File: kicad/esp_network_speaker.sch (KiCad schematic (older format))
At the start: 13 parts, among them U1 ESP12, U2 23A1024, U3 PCM5100A

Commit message: kicad project updated
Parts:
- removed U1: ESP12, ESP12:ESP12, symbol ESP12
- removed U2: 23A1024, SMD_Packages:SOIC-8-N, symbol 23A1024
- added C11, C12: 100nF, Capacitors_SMD:C_0603_HandSoldering, symbol C_Small
- added R1, R2: 470, Resistors_SMD:R_0603_HandSoldering, symbol R_Small
- added R3: 10k, Resistors_SMD:R_0603_HandSoldering, symbol R_Small
- added U1: 23LC1024, Housings_SOIC:SOIC-8_3.9x4.9mm_Pitch1.27mm, symbol 23LC1024
- added U2: ESP12, ESP12:ESP12, symbol ESP12
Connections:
- net labels added: DAC_DATA, DAC_OUTM, ESP12_CLK, ESP12_CS, ESP12_MISO, ESP12_MOSI
- net labels removed: DAC_DIN, DAC_SCK
- wire segments 42 -> 59
- no-connect marks 0 -> 1
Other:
- moved on the sheet: C1, C10, C2, C3, C4, C5, C6, C7, C8, C9, U3

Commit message: wip, most of the components are in now
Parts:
- added C13: 100nF, Capacitors_SMD:C_0603_HandSoldering, symbol C_Small
- added D1, D2: LED, Resistors_SMD:R_0603_HandSoldering, symbol LED
- added Q?: Q_NPN_BCE, symbol Q_NPN_BCE
- added R4, R5: 220, Resistors_SMD:R_0603_HandSoldering, symbol R_Small
- added R6, R7, R8, R9: 1k, Resistors_SMD:R_0603_HandSoldering, symbol R_Small
- added SW1: SW_PUSH, Buttons_Switches_SMD:SW_SPST_FSMSM, symbol SW_PUSH
- added U4: TSR_1-2433, traco:TSR-1, symbol TSR_1-2433
- added U5: M74VHC1GT125, TO_SOT_Packages_SMD:SOT-353, symbol M74VHC1GT125
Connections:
- net +3V3: now also C13.1, R6.1, R7.1, R9.2, U4.3 (Vout), U5.5 (VCC)
- net DAC_BCK: now also Q?.2 (C), R6.2
- net DAC_DATA: now also U5.4 (OUT)
- net DAC_LRCK: now also R7.2
- net ESP12_CS: now also R8.1
- net GND: now also C13.2, R4.1, R5.1, R8.2, U4.2 (GND), U5.3 (GND)
- net LEDA: now reaches U2.19 (GPIO4)
- net LEDA: now also D2.2 (A)
- net LEDB: now reaches U2.20 (GPIO5)
- net LEDB: now also D1.2 (A)
- net ESP12_TX: now reaches U2.22 (GPIO1/UART0_TXD)
- net at U2.3 (ENABLE): now also R9.1
- new net: D2.1 (K), R5.2
- new net: D1.1 (K), R4.2
- new net +BATT: U4.1 (Vin)
- new net PROG_TX: U5.2 (IN)

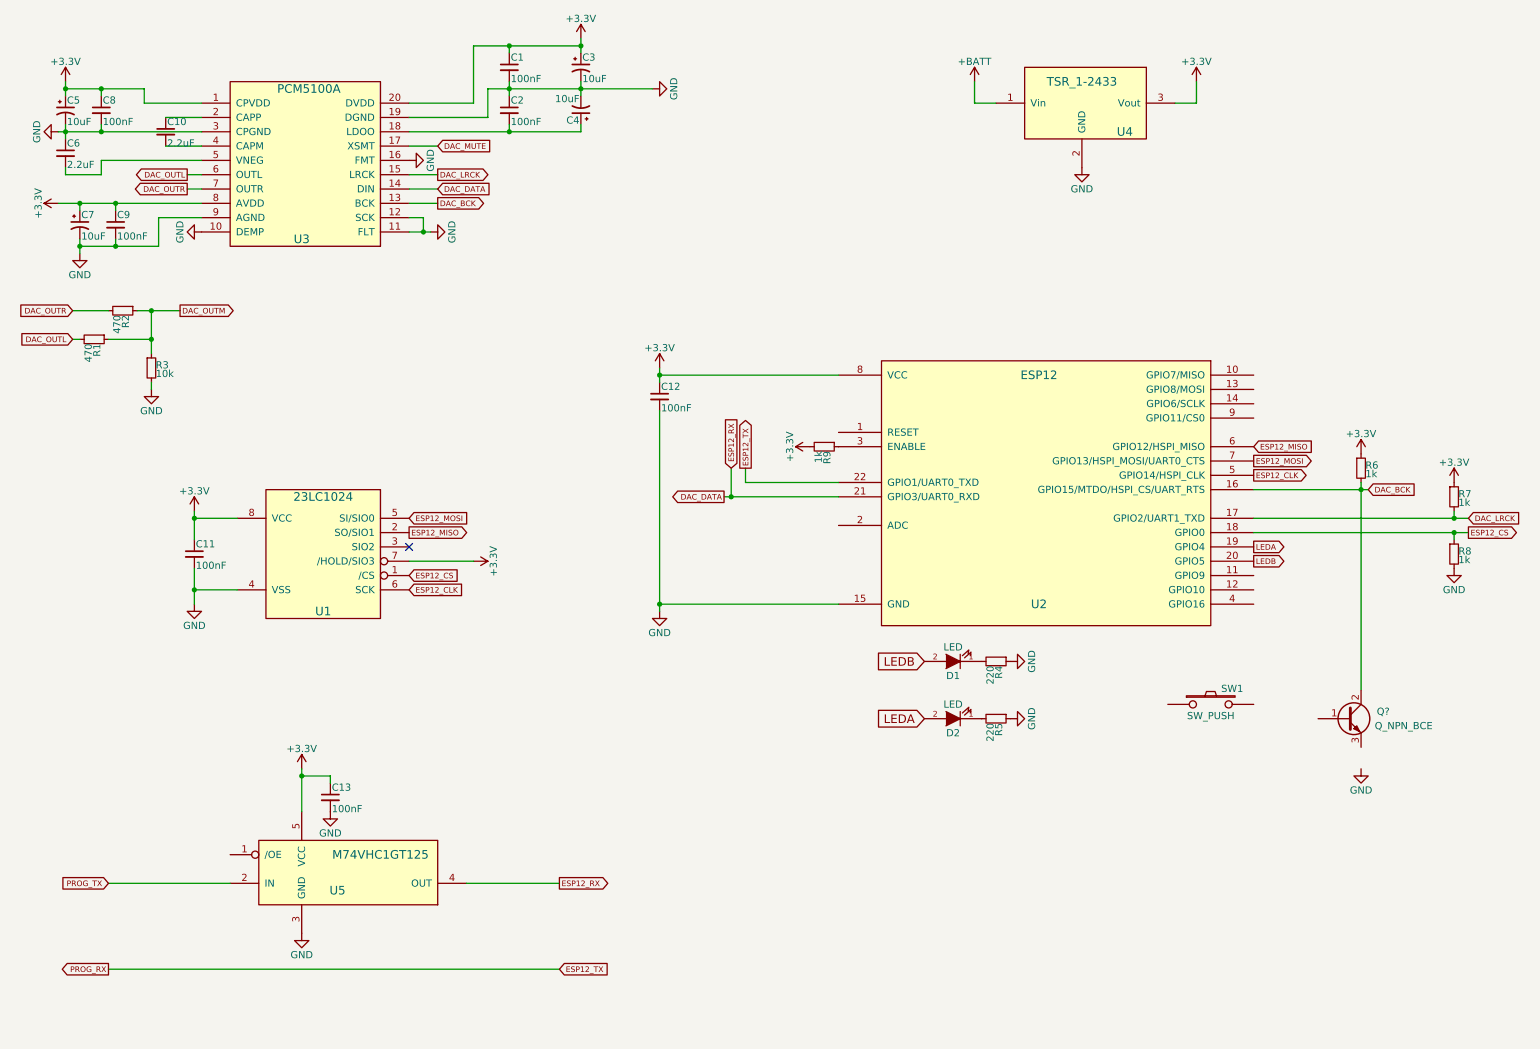
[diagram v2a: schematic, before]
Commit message: schematic finished, some placement done
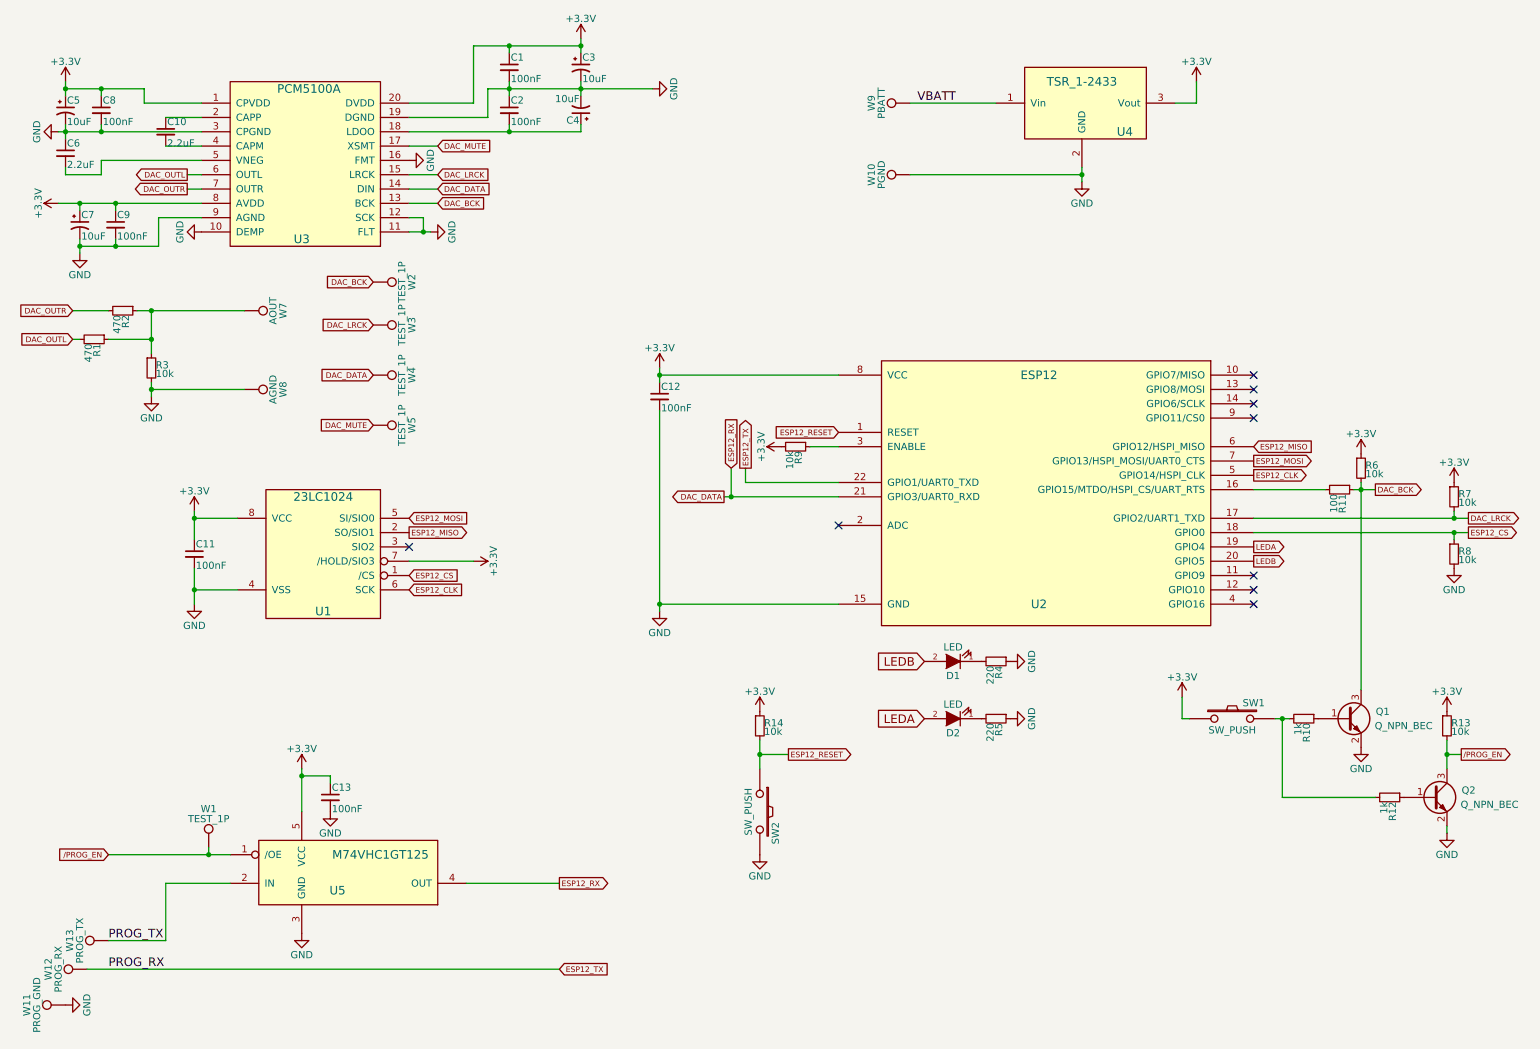
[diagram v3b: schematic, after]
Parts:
- removed Q?: Q_NPN_BCE, symbol Q_NPN_BCE
- added Q1, Q2: Q_NPN_BEC, TO_SOT_Packages_SMD:SOT-23, symbol Q_NPN_BEC
- added R10, R12: 1k, Resistors_SMD:R_0603_HandSoldering, symbol R_Small
- added R11: 100, Resistors_SMD:R_0603_HandSoldering, symbol R_Small
- added R13, R14: 10k, Resistors_SMD:R_0603_HandSoldering, symbol R_Small
- added SW2: SW_PUSH, Buttons_Switches_SMD:SW_SPST_FSMSM, symbol SW_PUSH
- added W1, W2, W3, W4, W5: TEST_1P, Measurement_Points:Measurement_Point_Round-SMD-Pad_Small, symbol TEST_1P
- added W10: PGND, Measurement_Points:Measurement_Point_Round-SMD-Pad_Big, symbol TEST_1P
- added W11: PROG_GND, Measurement_Points:Measurement_Point_Round-SMD-Pad_Big, symbol TEST_1P
- added W12: PROG_RX, Measurement_Points:Measurement_Point_Round-SMD-Pad_Big, symbol TEST_1P
- added W13: PROG_TX, Measurement_Points:Measurement_Point_Round-SMD-Pad_Big, symbol TEST_1P
- added W7: AOUT, Measurement_Points:Measurement_Point_Round-SMD-Pad_Big, symbol TEST_1P
- added W8: AGND, Measurement_Points:Measurement_Point_Round-SMD-Pad_Big, symbol TEST_1P
- added W9: PBATT, Measurement_Points:Measurement_Point_Round-SMD-Pad_Big, symbol TEST_1P
- R6, R7, R8, R9: value 1k -> 10k
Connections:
- net +3V3: now also SW1.1, R13.1, R14.1
- net DAC_BCK: now also Q1.3 (C), R11.1, W2.1; no longer U2.16 (GPIO15/MTDO/HSPI_CS/UART_RTS)
- net DAC_DATA: now also W4.1
- net DAC_LRCK: now also W3.1
- net DAC_MUTE: now also W5.1
- net ESP12_TX: now also W12.1
- net GND: now also Q1.2 (E), Q2.2 (E), SW2.2, W10.1, W11.1, W8.1
- net PROG_TX: now also W13.1
- net ESP12_RESET: now reaches U2.1 (RESET)
- net ESP12_RESET: now also R14.2, SW2.1
- net at SW1.2: now also R10.2, R12.2
- net /PROG_EN: now reaches U5.1 (/OE)
- net /PROG_EN: now also Q2.3 (C), R13.2, W1.1
- net +BATT renamed VBATT
- net VBATT: now also W9.1
- net DAC_OUTM: no longer names the net of R1.1, R2.1, R3.1
- net DAC_OUTM: now also W7.1
- new net: R11.2, U2.16 (GPIO15/MTDO/HSPI_CS/UART_RTS)
- new net: Q1.1 (B), R10.1
- new net: Q2.1 (B), R12.1
- no-connect marks 1 -> 9
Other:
- moved on the sheet: R9, SW1

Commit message: routing in progress, first pass almost finished
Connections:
- net DAC_MUTE: now also U2.11 (GPIO9)
- no-connect marks 9 -> 8
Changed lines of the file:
@@
 Wire Wire Line
 	1750 7100 1350 7100
-NoConn ~ 9350 4550
 NoConn ~ 9350 4650
 NoConn ~ 9350 4750
@@
 Text Label 7000 1250 0    60   ~ 0
 VBATT
+Text GLabel 9350 4550 2    39   Output ~ 0
+DAC_MUTE
 $EndSCHEMATC
